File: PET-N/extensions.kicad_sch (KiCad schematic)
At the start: 78 parts, among them SW1 KP "=", SW10 KP "0", SW11 R SHIFT, SW12 ">", SW14 "]", SW15 "@", SW16 L SHIFT, SW17 KP "+", SW18 KP "2", SW2 KP ".", SW20 "?", SW21 ",", SW22 "N", SW23 "V", SW24 "X", SW25 KP "3", SW26 KP "1", SW27 RETURN, SW28 ";", SW29 "M", SW3 NC ($10), SW30 "B", SW31 "C", SW32 "Z", SW320 S LOCK, SW33 KP "*", SW34 KP "5", SW36 ":", SW37 "K", SW38 "H", SW39 "F", SW4 STOP, SW40 "S", SW41 KP "6", SW42 KP "4", SW44 "L", SW45 "J", SW46 "G", SW47 "D", SW48 "A", SW49 KP "/", SW5 "<", SW50 KP "8", SW52 "P", SW53 "I", SW54 "Y", SW55 "R", SW56 "W", SW57 KP "9", SW58 KP "7", SW59 U ARROW, SW6 SPACE, SW60 "O", SW61 "U", SW62 "T", SW63 "E", SW64 "Q", SW65 INS/DEL, SW66 UP/DOWN, SW67 NC ($0A), SW68 ")", SW69 "\", SW7 "[", SW70 "'", SW71 "$", SW72 QUOTE, SW73 LEFT/RIGHT, SW74 CLR/HOME, SW75 B ARROW, SW76 "(", SW77 "&", SW78 "%", SW79 "#", SW8 OFF/RVS, SW80 "!", SW9 KP "-", U1 74LS145

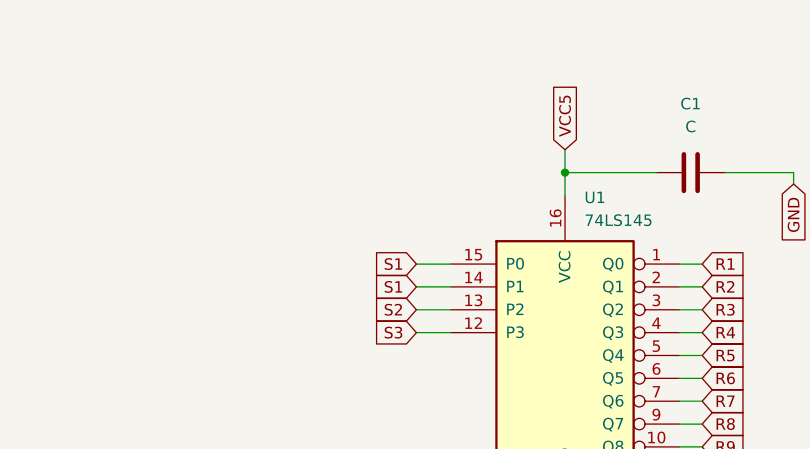
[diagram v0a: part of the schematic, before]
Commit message: add joystick footprints
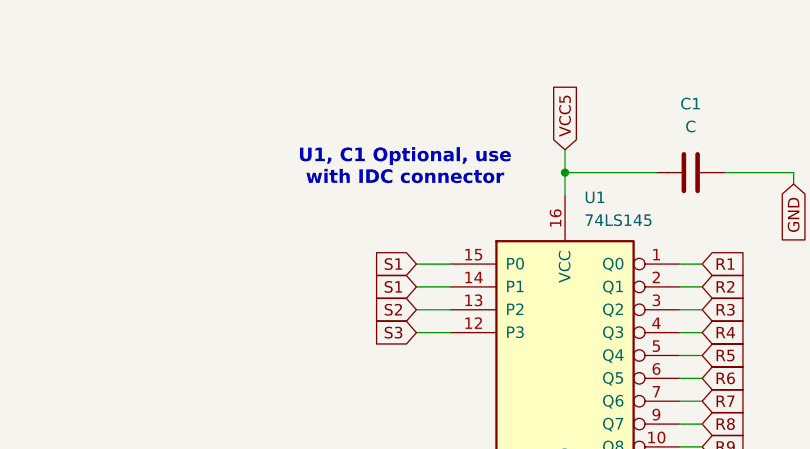
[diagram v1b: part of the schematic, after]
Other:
- note added: "U1, C1 Optional, use with IDC connector"
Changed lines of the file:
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@@
+		)
+	)
+	(text "U1, C1 Optional, use\nwith IDC connector"
+		(exclude_from_sim no)
+		(at 208.28 32.512 0)
+		(effects
+			(font
+				(size 1.5 1.5)
+				(thickness 0.3)
+				(bold yes)
+			)
 		)
 	)

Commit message: work on R3 of keyboard pcb
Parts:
- removed C1: C, Capacitor_THT:C_Disc_D4.3mm_W1.9mm_P5.00mm, symbol Device:C
- removed U1: 74LS145, Package_DIP:DIP-16_W7.62mm, symbol 74xx:74LS145
- added R100, R101, R102, R103, R104, R105, R106, R107, R108, R109, R110, R111, R112, R113, R114, R115, R116, R117, R118, R119, R120, R121, R122, R123, R124, R125, R50, R51, R52, R53, R54, R55, R56, R57, R58, R59, R60, R61, R62, R63, R64, R65, R66, R67, R68, R69, R70, R71, R72, R73, R74, R75, R76, R77, R78, R79, R80, R81, R82, R83, R84, R85, R86, R87, R88, R89, R90, R91, R92, R93, R94, R95, R96, R97, R98, R99: 390, Resistor_SMD:R_0805_2012Metric, symbol Device:R
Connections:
- net at SW11.3 (K): now also R115.1
- net HI7: now reaches SW11.4 (A)
- net HI7: now also SW21.4 (A), SW37.4 (A), SW53.4 (A), SW69.4 (A)
- net at SW70.3 (K): now also R56.1
- net HI5: now reaches SW70.4 (A)
- net HI5: now also SW22.4 (A), SW28.4 (A), SW38.4 (A), SW54.4 (A), SW6.4 (A)
- net at SW34.3 (K): now also R101.1
- net HI1: now reaches SW34.4 (A)
- net HI1: now also SW18.4 (A), SW2.4, SW24.4 (A), SW36.4 (A), SW40.4 (A), SW50.4 (A), SW52.4 (A), SW56.4 (A), SW66.4 (A), SW68.4 (A), SW72.4 (A)
- net at SW65.3 (K): now also R67.1
- net HI3: now reaches SW65.4 (A)
- net HI3: now also SW1.4 (A), SW17.4 (A), SW23.4 (A), SW33.4 (A), SW39.4 (A), SW49.4 (A), SW5.4 (A), SW55.4 (A), SW7.4 (A), SW71.4 (A)
- net at SW18.3 (K): now also R119.1
- net at SW72.3 (K): now also R52.1
- net at SW39.3 (K): now also R90.1
- net at SW1.3 (K): now also R125.1
- net at SW47.3 (K): now also R89.1
- net HI2: now reaches SW47.4 (A)
- net HI2: now also SW25.4 (A), SW31.4 (A), SW41.4 (A), SW57.4 (A), SW59.4 (A), SW63.4 (A), SW73.4 (A), SW75.4 (A), SW79.4 (A), SW9.4 (A)
- net at SW5.3 (K): now also R80.1
- net at SW49.3 (K): now also R85.1
- net at SW78.3 (K): now also R55.1
- net HI4: now reaches SW78.4 (A)
- net HI4: now also SW12.4 (A), SW14.4 (A), SW15.4 (A), SW16.4 (A), SW30.4 (A), SW320.4, SW46.4 (A), SW62.4 (A), SW67.4, SW8.4 (A)
- net at SW32.3 (K): now also R105.1
- net HI0: now reaches SW32.4 (A)
- net HI0: now also SW26.4 (A), SW42.4 (A), SW44.4 (A), SW48.4 (A), SW58.4 (A), SW60.4 (A), SW64.4 (A), SW74.4 (A), SW76.4 (A), SW80.4 (A)
- net at SW64.3 (K): now also R69.1
- net at SW48.3 (K): now also R87.1
- net at SW15.3 (K): now also R50.1
- net at SW2.3: now also R123.1
- net at SW55.3 (K): now also R72.1
- net at SW8.3 (K): now also R68.1
- net at SW4.3 (K): now also R97.1
- net at SW37.3 (K): now also R94.1
- net at SW71.3 (K): now also R54.1
- net at SW3.3: now also R117.1
- net HI6: now reaches SW3.4
- net HI6: now also SW20.4 (A), SW29.4 (A), SW45.4 (A), SW61.4 (A), SW77.4 (A)
- net at SW56.3 (K): now also R70.1
- net at SW75.3 (K): now also R61.1
- net at SW6.3 (K): now also R116.1
- net at SW69.3 (K): now also R58.1
- net at SW24.3 (K): now also R106.1
- net at SW16.3 (K): now also R104.1
- net at SW320.3: now also R86.1
- net at SW36.3 (K): now also R96.1
- net at SW62.3 (K): now also R73.1
- net at SW20.3 (K): now also R114.1
- net at SW17.3 (K): now also R121.1
- net at SW45.3 (K): now also R93.1
- net at SW66.3 (K): now also R65.1
- net at SW50.3 (K): now also R83.1
- net at SW7.3 (K): now also R62.1
- net at SW31.3 (K): now also R107.1
- net at SW52.3 (K): now also R78.1
- net at SW46.3 (K): now also R91.1
- net at SW67.3: now also R99.1
- net at SW59.3 (K): now also R79.1
- net at SW14.3 (K): now also R63.1
- net at SW73.3 (K): now also R66.1
- net at SW33.3 (K): now also R103.1
- net at SW25.3 (K): now also R120.1
- net at SW60.3 (K): now also R77.1
- net at SW10.3 (K): now also R122.1
- net at SW27.3 (K): now also R98.1
- net at SW38.3 (K): now also R92.1
- net at SW29.3 (K): now also R111.1
- net at SW9.3 (K): now also R124.1
- net at SW26.3 (K): now also R118.1
- net at SW63.3 (K): now also R71.1
- net at SW68.3 (K): now also R60.1
- net at SW21.3 (K): now also R112.1
- net at SW22.3 (K): now also R110.1
- net at SW53.3 (K): now also R76.1
- net at SW41.3 (K): now also R102.1
- net at SW58.3 (K): now also R82.1
- net at SW76.3 (K): now also R59.1
- net at SW40.3 (K): now also R88.1
- net at SW54.3 (K): now also R74.1
- net at SW61.3 (K): now also R75.1
- net at SW28.3 (K): now also R113.1
- net at SW80.3 (K): now also R51.1
- net at SW79.3 (K): now also R53.1
- net at SW77.3 (K): now also R57.1
- net at SW57.3 (K): now also R84.1
- net at SW30.3 (K): now also R109.1
- net at SW12.3 (K): now also R81.1
- net at SW42.3 (K): now also R100.1
- net at SW23.3 (K): now also R108.1
- net at SW44.3 (K): now also R95.1
- net at SW74.3 (K): now also R64.1
- new net: R77.2, R78.2, R79.2, R80.2, R81.2
- new net LO0: R50.2, R64.2, R65.2, R66.2, R67.2
- new net LO1: R68.2, R82.2, R83.2, R84.2, R85.2
- new net LO11: R95.2, R96.2
- new net LO2: R100.2, R101.2, R102.2, R103.2, R86.2, R97.2, R98.2
- new net LO3: R104.2, R113.2, R114.2, R115.2, R118.2, R119.2, R120.2, R121.2
- new net LO4: R116.2, R117.2, R122.2, R123.2, R124.2, R125.2, R99.2
- new net LO5: R51.2, R52.2, R53.2, R54.2, R55.2, R56.2, R57.2, R58.2
- new net LO6: R69.2, R70.2, R71.2, R72.2, R73.2, R74.2, R75.2, R76.2
- new net LO7: R87.2, R88.2, R89.2, R90.2, R91.2, R92.2, R93.2, R94.2
- new net LO8: R105.2, R106.2, R107.2, R108.2, R109.2, R110.2, R111.2, R112.2
- new net LO9: R59.2, R60.2, R61.2, R62.2, R63.2
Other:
- note removed: "1"
- note removed: "2"
- note removed: "3"
- note removed: "4"
- note removed: "5"
- note removed: "6"
- note removed: "7"
- note removed: "8"
- note removed: "A"
- note removed: "B"
- note removed: "C"
- note removed: "D"
- note removed: "E"
- note removed: "F"
- note removed: "G"
- note removed: "H"
- note removed: "I"
- note removed: "J"
- note removed: "LOCK"
- note removed: "R1 R2 R3 R4 R5 R6 R7 R8 R9 R10"
- note removed: "U1, C1 Optional, use with IDC connector"
- moved on the sheet: SW10B, SW11B, SW12B, SW14B, SW15B, SW16B, SW17B, SW18B, SW1B, SW20B, SW21B, SW22B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

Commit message: initial placement
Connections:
- net LO10: now also R77.2, R78.2, R79.2, R80.2, R81.2
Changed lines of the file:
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@@
-	(wire
-		(pts
-			(xy 27.305 90.805) (xy 33.02 90.805)
-		)
-		(stroke
-			(width 0)
-			(type default)
-		)
-	)
 	(wire
 		(pts
@@
 		)
 		(stroke
+			(width 0)
+			(type default)
+		)
+	)
+	(wire
+		(pts
+			(xy 26.67 90.805) (xy 33.02 90.805)
+		)
+		(stroke

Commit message: PET-N r3
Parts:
- R100, R101, R102, R103, R104, R105, R106, R107, R108, R109, R110, R111, R112, R113, R114, R115, R116, R117, R118, R119, R120, R121, R122, R123, R124, R125, R50, R51, R52, R53, R54, R55, R56, R57, R58, R59, R60, R61, R62, R63, R64, R65, R66, R67, R68, R69, R70, R71, R72, R73, R74, R75, R76, R77, R78, R79, R80, R81, R82, R83, R84, R85, R86, R87, R88, R89, R90, R91, R92, R93, R94, R95, R96, R97, R98, R99: LCSC (none) -> C17655
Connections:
- net HI0: now also SW10.4 (A)
